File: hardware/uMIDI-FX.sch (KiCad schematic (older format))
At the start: 0 parts

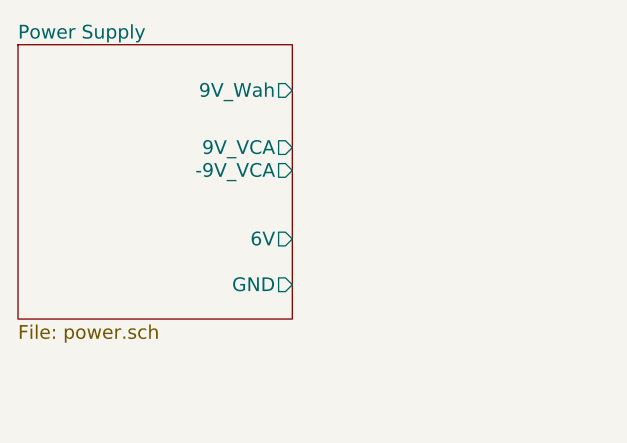
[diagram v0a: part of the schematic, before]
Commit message: Draw VCA power supply
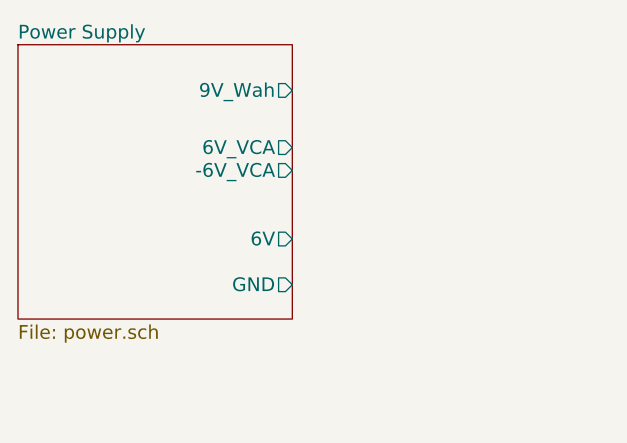
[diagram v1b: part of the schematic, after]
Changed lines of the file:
@@
 F1 "power.sch" 60
 F2 "9V_Wah" O R 2450 1450 60
-F3 "-9V_VCA" O R 2450 1800 60
-F4 "9V_VCA" O R 2450 1700 60
+F3 "-6V_VCA" O R 2450 1800 60
+F4 "6V_VCA" O R 2450 1700 60
 F5 "GND" O R 2450 2300 60
 F6 "6V" O R 2450 2100 60

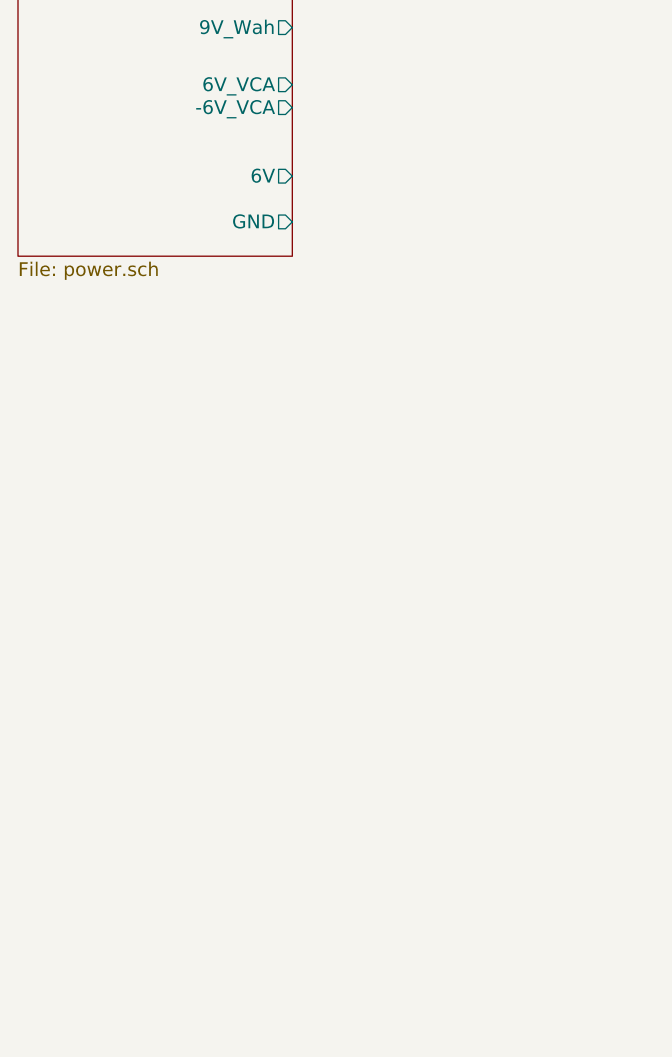
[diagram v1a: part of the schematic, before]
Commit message: Stub wah subcircuit
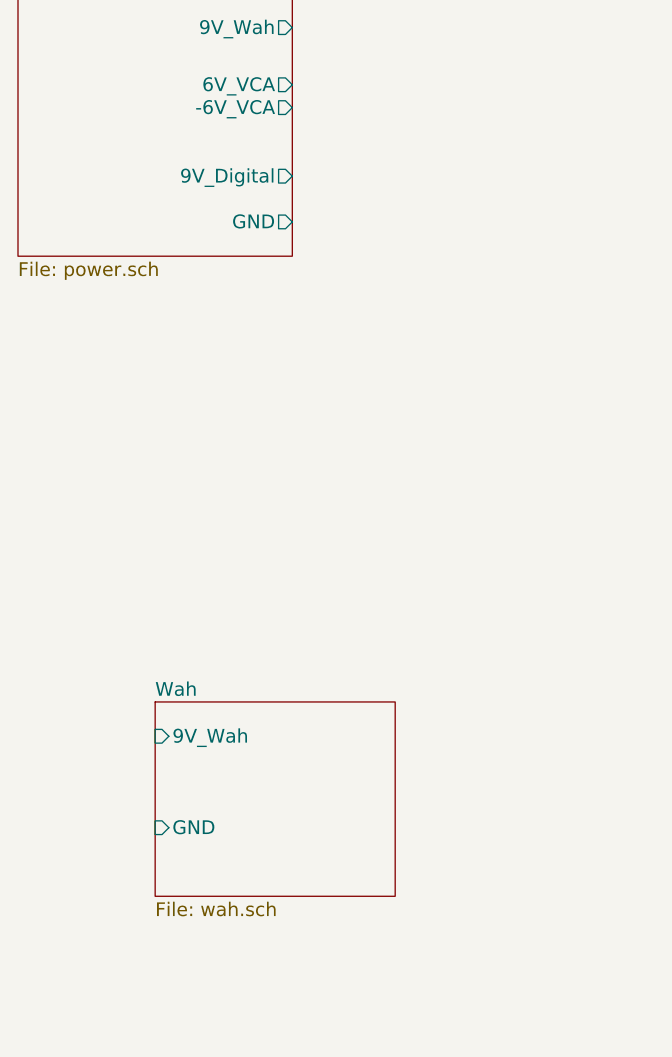
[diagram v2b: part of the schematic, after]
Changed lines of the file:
@@
 $Descr A4 11693 8268
 encoding utf-8
-Sheet 1 4
+Sheet 1 5
 Title ""
 Date ""
@@
 F4 "6V_VCA" O R 2450 1700 60
 F5 "GND" O R 2450 2300 60
-F6 "6V" O R 2450 2100 60
+F6 "9V_Digital" O R 2450 2100 60
+$EndSheet
+$Sheet
+S 1850 4400 1050 850
+U 54D5349F
+F0 "Wah" 60
+F1 "wah.sch" 60
+F2 "9V_Wah" I L 1850 4550 60
+F3 "GND" I L 1850 4950 60
 $EndSheet
 $EndSCHEMATC

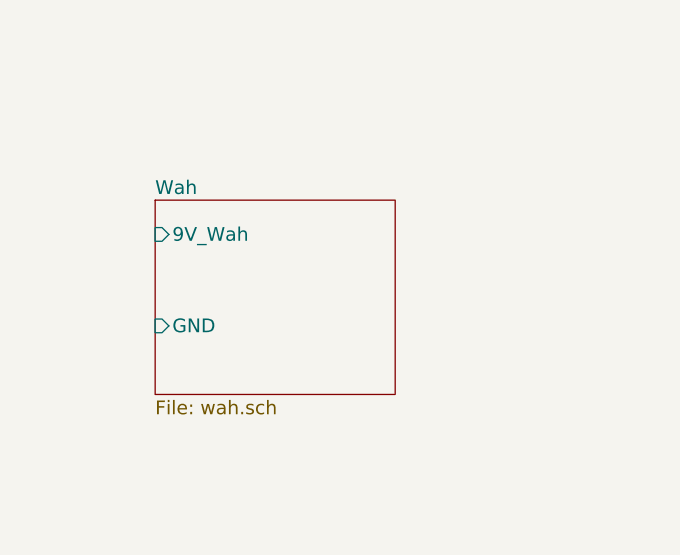
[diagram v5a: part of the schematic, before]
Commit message: Complete wah circuit
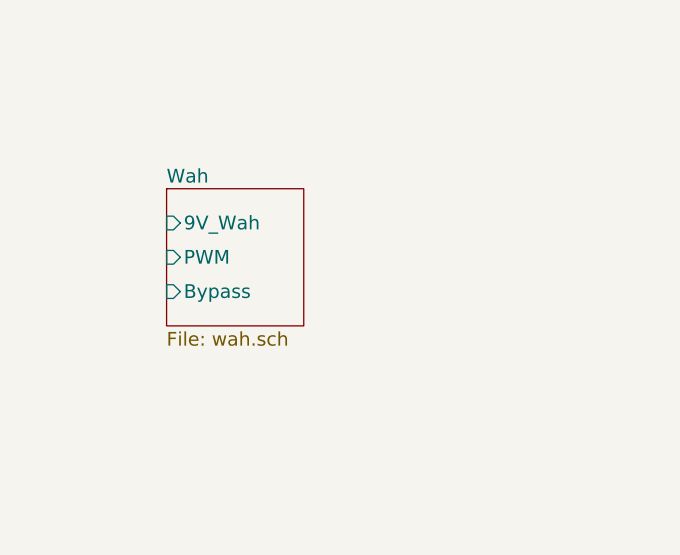
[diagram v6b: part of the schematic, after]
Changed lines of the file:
@@
 $EndSheet
 $Sheet
-S 1850 4400 1050 850
+S 1900 4350 600  600
 U 54D5349F
 F0 "Wah" 60
 F1 "wah.sch" 60
-F2 "9V_Wah" I L 1850 4550 60
-F3 "GND" I L 1850 4950 60
+F2 "9V_Wah" I L 1900 4500 60
+F4 "PWM" I L 1900 4650 60
+F5 "Bypass" I L 1900 4800 60
 $EndSheet
 $EndSCHEMATC

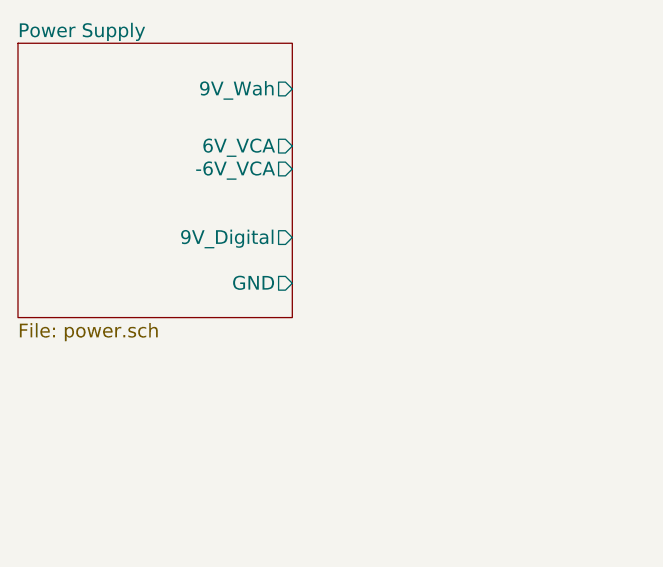
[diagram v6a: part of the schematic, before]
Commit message: Remove GND label from power supply
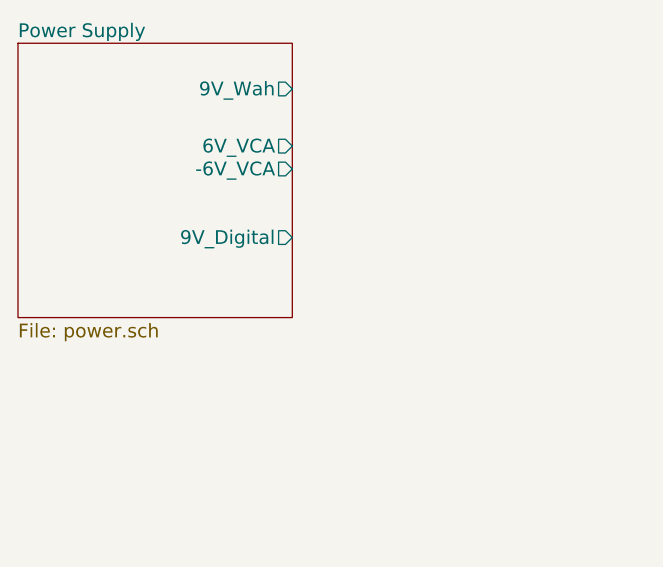
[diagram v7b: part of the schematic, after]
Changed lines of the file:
@@
 F3 "-6V_VCA" O R 2450 1800 60
 F4 "6V_VCA" O R 2450 1700 60
-F5 "GND" O R 2450 2300 60
 F6 "9V_Digital" O R 2450 2100 60
 $EndSheet

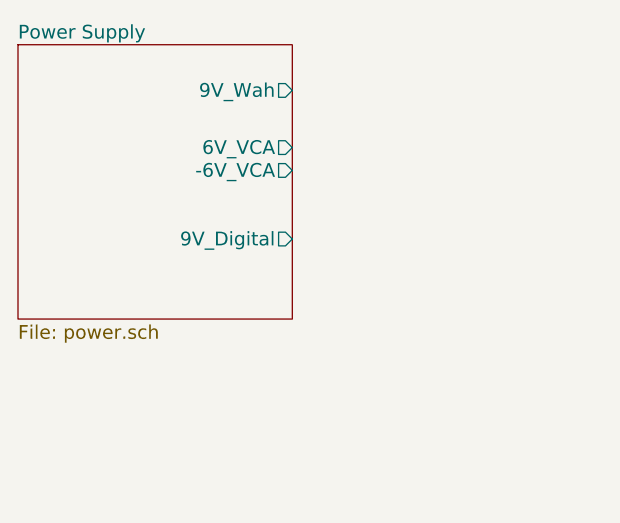
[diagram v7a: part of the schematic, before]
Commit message: Use global label for digital (noisy) 9V
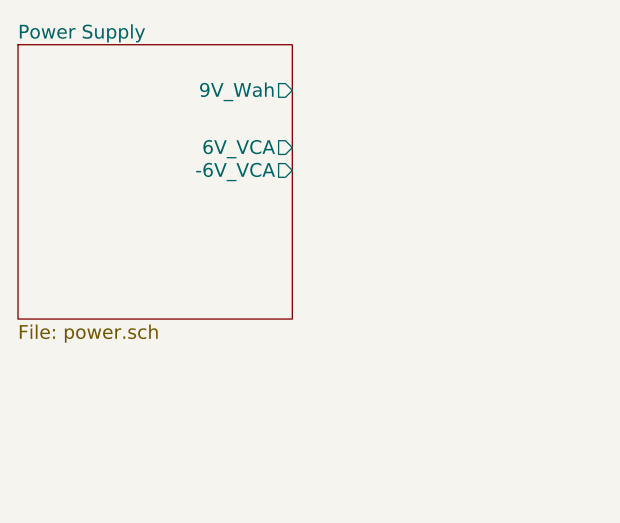
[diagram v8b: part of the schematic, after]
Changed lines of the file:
@@
 F3 "-6V_VCA" O R 2450 1800 60
 F4 "6V_VCA" O R 2450 1700 60
-F6 "9V_Digital" O R 2450 2100 60
 $EndSheet
 $Sheet
